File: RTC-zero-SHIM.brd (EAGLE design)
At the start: 30 x 65 mm, 16 parts, among them IC1 DS3231/SO, IC2 DS3231M

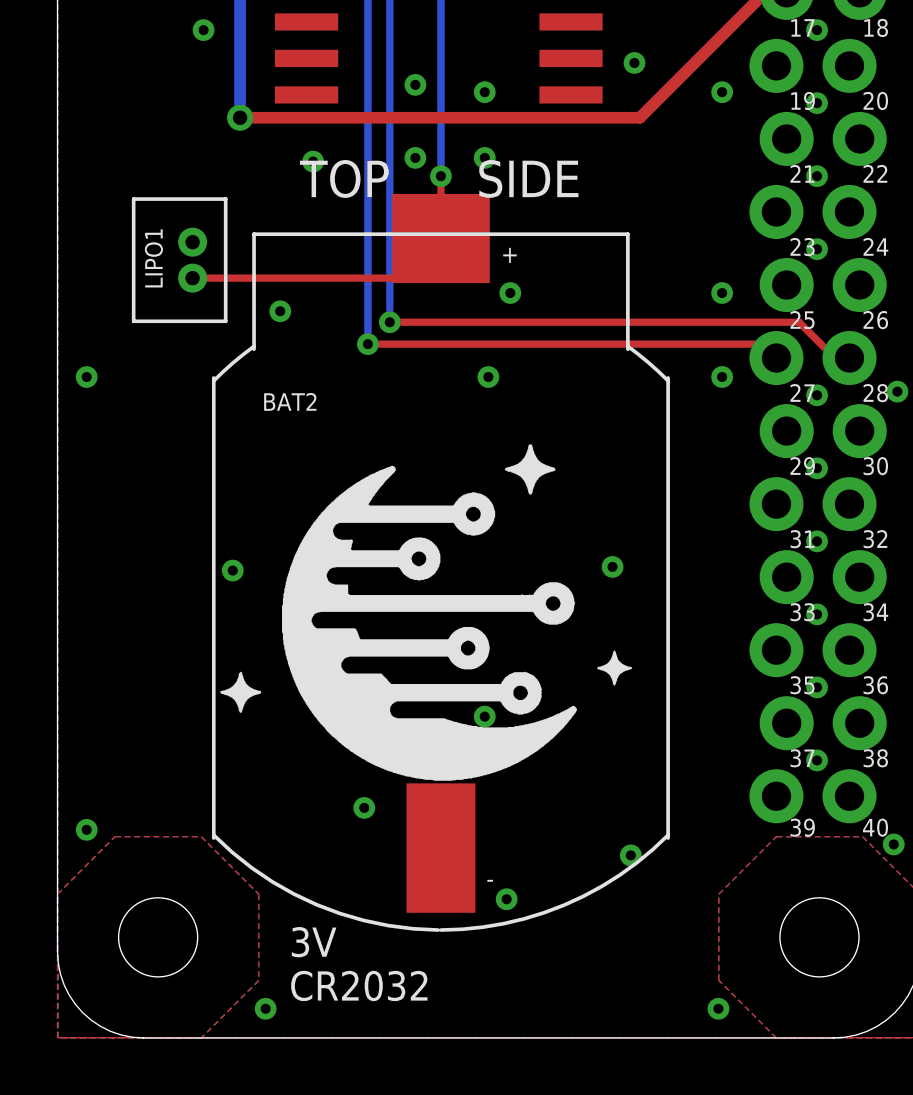
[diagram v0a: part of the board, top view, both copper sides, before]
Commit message: Moved battery holder and lipo connector a bit down to improve compatibility with other boards.
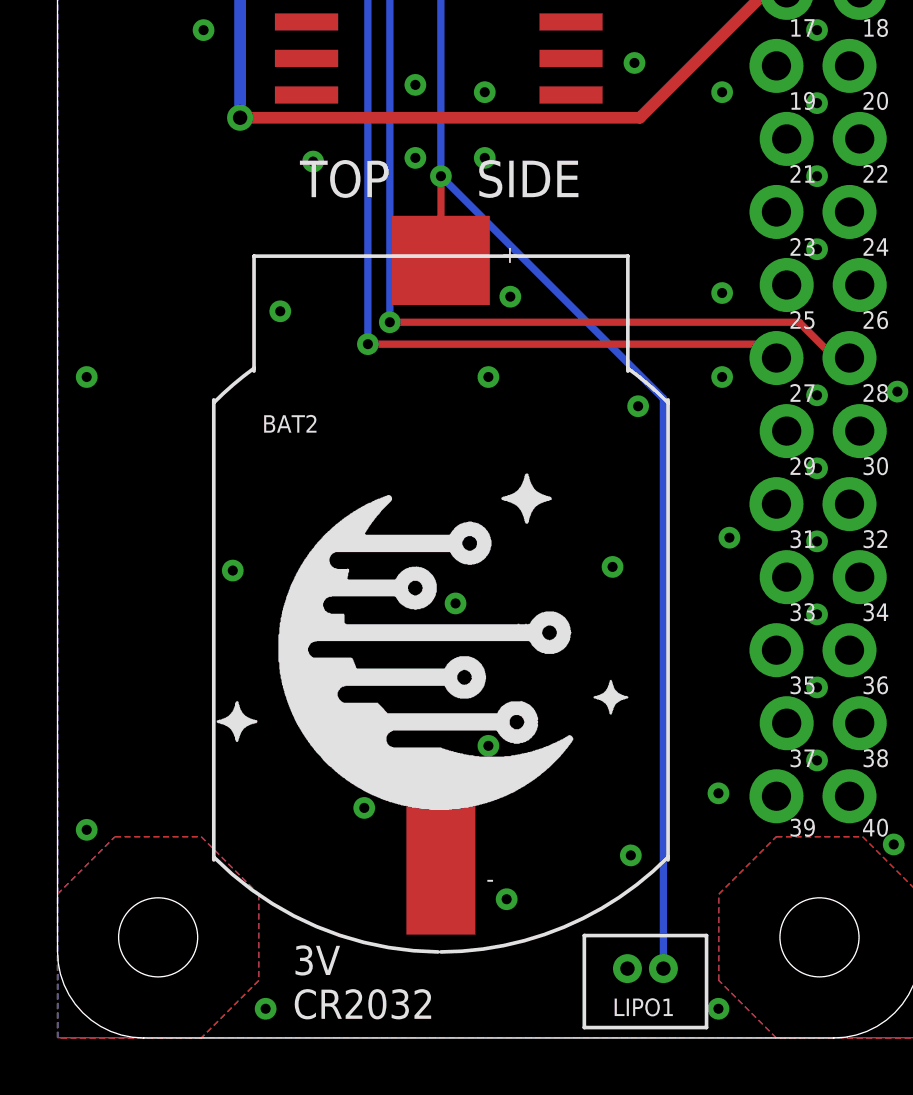
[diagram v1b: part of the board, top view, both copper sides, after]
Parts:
- moved LIPO1 29.2 mm to (20.4, 2.41), turned to 180 degrees
- moved LOGO4 1.02 mm to (4.75, 7.02)
- moved BAT2 0.76 mm to (13.3, 14.2)
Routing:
- net VBAT: track 25.0 -> 47.3 mm
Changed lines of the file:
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@@
 <text x="18.976" y="39.147" size="1.016" layer="22" font="vector" ratio="12" rot="MR0">I2C bus selection</text>
 <rectangle x1="23.912" y1="55.397" x2="26.452" y2="57.937" layer="21"/>
-<text x="8.054" y="1.301" size="1.016" layer="21" font="vector" ratio="12">3V
+<text x="8.181" y="0.666" size="1.016" layer="21" font="vector" ratio="12">3V
 CR2032</text>
 <circle x="7.165" y="42.322" radius="0.127" width="0.2032" layer="21"/>
@@
 <attribute name="VALUE" x="13.3611" y="41.941" size="0.02" layer="28" rot="MR0"/>
 </element>
-<element name="BAT2" library="BS-8-1" package="BS-8-1" value="BS-8-1" x="13.335" y="14.954" smashed="yes" rot="R180">
-<attribute name="NAME" x="7.112" y="21.812" size="0.6096" layer="25" font="vector"/>
-<attribute name="VALUE" x="7.112" y="20.669" size="0.6096" layer="27" font="vector"/>
+<element name="BAT2" library="BS-8-1" package="BS-8-1" value="BS-8-1" x="13.335" y="14.192" smashed="yes" rot="R180">
+<attribute name="NAME" x="7.112" y="21.05" size="0.6096" layer="25" font="vector"/>
+<attribute name="VALUE" x="7.112" y="19.907" size="0.6096" layer="27" font="vector"/>
 </element>
 <element name="LOGO1" library="_my_logos" package="MFDEC_SQ_8MM" value="MFDECLOGO_SQ_8MM" x="7.927" y="51.339" smashed="yes"/>
 <element name="LOGO2" library="_my_logos" package="MFDEC_L_30MM" value="MFDECLOGO_L_30MM" x="-4.138" y="-7.97" smashed="yes" rot="MR90"/>
 <element name="LOGO3" library="_my_logos" package="RSNURL_QR_10MM" value="RSNURL_QR_10MM" x="18.087" y="51.339" smashed="yes" rot="MR0"/>
-<element name="LIPO1" library="PiB_connectors" package="_MOLEX-0530470210_VERT_PITCH-1.25MM" package3d_urn="urn:adsk.eagle:package:2973718/3" value="Molex VERT 1.25mm pitch" x="4.699" y="27.051" smashed="yes" rot="R90">
-<attribute name="DATASHEET_CONNECTOR1" value="https://www.molex.com/pdm_docs/sd/530470210_sd.pdf" x="4.699" y="27.051" size="1.778" layer="27" rot="R90" display="off"/>
-<attribute name="DATASHEET_CONNECTOR2" value="https://www.molex.com/pdm_docs/sd/510210700_sd.pdf" x="4.699" y="27.051" size="1.778" layer="27" rot="R90" display="off"/>
-<attribute name="DATASHEET_CRIMP" value="https://www.molex.com/pdm_docs/sd/500798000_sd.pdf" x="4.699" y="27.051" size="1.778" layer="27" rot="R90" display="off"/>
-<attribute name="DISTLINK_CONNECTOR1" value="https://www.digikey.com/products/en?keywords=WM1731-ND" x="4.699" y="27.051" size="1.778" layer="27" rot="R90" display="off"/>
-<attribute name="DISTLINK_CONNECTOR2" value="https://www.digikey.com/products/en?keywords=WM1720-ND" x="4.699" y="27.051" size="1.778" layer="27" rot="R90" display="off"/>
-<attribute name="DISTLINK_CRIMP" value="https://www.digikey.com/products/en?keywords=WM1142CT-ND" x="4.699" y="27.051" size="1.778" layer="27" rot="R90" display="off"/>
-<attribute name="DISTPN_CONNECTOR1" value="WM1731-ND" x="4.699" y="27.051" size="1.778" layer="27" rot="R90" display="off"/>
-<attribute name="DISTPN_CONNECTOR2" value="WM1720-ND" x="4.699" y="27.051" size="1.778" layer="27" rot="R90" display="off"/>
-<attribute name="DISTPN_CRIMP" value="WM1142CT-ND" x="4.699" y="27.051" size="1.778" layer="27" rot="R90" display="off"/>
-<attribute name="DIST_CONNECTOR1" value="Digikey" x="4.699" y="27.051" size="1.778" layer="27" rot="R90" display="off"/>
-<attribute name="DIST_CONNECTOR2" value="Digikey" x="4.699" y="27.051" size="1.778" layer="27" rot="R90" display="off"/>
-<attribute name="DIST_CRIMP" value="Digikey" x="4.699" y="27.051" size="1.778" layer="27" rot="R90" display="off"/>
-<attribute name="MFR_CONNECTOR1" value="Molex, LLC" x="4.699" y="27.051" size="1.778" layer="27" rot="R90" display="off"/>
-<attribute name="MFR_CONNECTOR2" value="Molex, LLC" x="4.699" y="27.051" size="1.778" layer="27" rot="R90" display="off"/>
-<attribute name="MFR_CRIMP" value="Molex, LLC" x="4.699" y="27.051" size="1.778" layer="27" rot="R90" display="off"/>
-<attribute name="MPN_CONNECTOR1" value="0530470210" x="4.699" y="27.051" size="1.778" layer="27" rot="R90" display="off"/>
-<attribute name="MPN_CONNECTOR2" value="51021-0200" x="4.699" y="27.051" size="1.778" layer="27" rot="R90" display="off"/>
-<attribute name="MPN_CRIMP" value="0500798000" x="4.699" y="27.051" size="1.778" layer="27" rot="R90" display="off"/>
-<attribute name="NAME" x="3.048" y="28.194" size="0.6096" layer="25" font="vector" rot="R270"/>
+<element name="LIPO1" library="PiB_connectors" package="_MOLEX-0530470210_VERT_PITCH-1.25MM" package3d_urn="urn:adsk.eagle:package:2973718/3" value="Molex VERT 1.25mm pitch" x="20.447" y="2.413" smashed="yes" rot="R180">
+<attribute name="DATASHEET_CONNECTOR1" value="https://www.molex.com/pdm_docs/sd/530470210_sd.pdf" x="20.447" y="2.413" size="1.778" layer="27" rot="R180" display="off"/>
+<attribute name="DATASHEET_CONNECTOR2" value="https://www.molex.com/pdm_docs/sd/510210700_sd.pdf" x="20.447" y="2.413" size="1.778" layer="27" rot="R180" display="off"/>
+<attribute name="DATASHEET_CRIMP" value="https://www.molex.com/pdm_docs/sd/500798000_sd.pdf" x="20.447" y="2.413" size="1.778" layer="27" rot="R180" display="off"/>
+<attribute name="DISTLINK_CONNECTOR1" value="https://www.digikey.com/products/en?keywords=WM1731-ND" x="20.447" y="2.413" size="1.778" layer="27" rot="R180" display="off"/>
+<attribute name="DISTLINK_CONNECTOR2" value="https://www.digikey.com/products/en?keywords=WM1720-ND" x="20.447" y="2.413" size="1.778" layer="27" rot="R180" display="off"/>
+<attribute name="DISTLINK_CRIMP" value="https://www.digikey.com/products/en?keywords=WM1142CT-ND" x="20.447" y="2.413" size="1.778" layer="27" rot="R180" display="off"/>
+<attribute name="DISTPN_CONNECTOR1" value="WM1731-ND" x="20.447" y="2.413" size="1.778" layer="27" rot="R180" display="off"/>
+<attribute name="DISTPN_CONNECTOR2" value="WM1720-ND" x="20.447" y="2.413" size="1.778" layer="27" rot="R180" display="off"/>
+<attribute name="DISTPN_CRIMP" value="WM1142CT-ND" x="20.447" y="2.413" size="1.778" layer="27" rot="R180" display="off"/>
+<attribute name="DIST_CONNECTOR1" value="Digikey" x="20.447" y="2.413" size="1.778" layer="27" rot="R180" display="off"/>
+<attribute name="DIST_CONNECTOR2" value="Digikey" x="20.447" y="2.413" size="1.778" layer="27" rot="R180" display="off"/>
+<attribute name="DIST_CRIMP" value="Digikey" x="20.447" y="2.413" size="1.778" layer="27" rot="R180" display="off"/>
+<attribute name="MFR_CONNECTOR1" value="Molex, LLC" x="20.447" y="2.413" size="1.778" layer="27" rot="R180" display="off"/>
+<attribute name="MFR_CONNECTOR2" value="Molex, LLC" x="20.447" y="2.413" size="1.778" layer="27" rot="R180" display="off"/>
+<attribute name="MFR_CRIMP" value="Molex, LLC" x="20.447" y="2.413" size="1.778" layer="27" rot="R180" display="off"/>
+<attribute name="MPN_CONNECTOR1" value="0530470210" x="20.447" y="2.413" size="1.778" layer="27" rot="R180" display="off"/>
+<attribute name="MPN_CONNECTOR2" value="51021-0200" x="20.447" y="2.413" size="1.778" layer="27" rot="R180" display="off"/>
+<attribute name="MPN_CRIMP" value="0500798000" x="20.447" y="2.413" size="1.778" layer="27" rot="R180" display="off"/>
+<attribute name="NAME" x="19.304" y="0.762" size="0.6096" layer="25" font="vector"/>
 </element>
 <element name="IC2" library="SparkFun-Clocks" library_urn="urn:adsk.eagle:library:511" package="SO08" package3d_urn="urn:adsk.eagle:package:37530/1" value="DS3231M" x="13.261" y="39.782" smashed="yes" rot="R270">
@@
 <attribute name="VALUE" x="14.785" y="38.004" size="0.6096" layer="27" font="vector" rot="R90"/>
 </element>
-<element name="LOGO4" library="_my_logos" package="MFDEC_L_10MM" value="MFDECLOGO_L_10MM" x="4.879" y="8.032" smashed="yes"/>
+<element name="LOGO4" library="_my_logos" package="MFDEC_L_10MM" value="MFDECLOGO_L_10MM" x="4.752" y="7.016" smashed="yes"/>
 </elements>
 <signals>
@@
 <contactref element="IC2" pad="6"/>
 <wire x1="17.861" y1="39.147" x2="16.061" y2="39.147" width="0.254" layer="1"/>
-<wire x1="13.335" y1="27.804" x2="11.957" y2="26.426" width="0.254" layer="1"/>
-<wire x1="11.957" y1="26.426" x2="4.699" y2="26.426" width="0.254" layer="1"/>
 <via x="13.335" y="29.972" extent="1-16" drill="0.35"/>
-<wire x1="13.335" y1="29.972" x2="13.335" y2="27.804" width="0.254" layer="1"/>
+<wire x1="13.335" y1="29.972" x2="13.335" y2="27.042" width="0.254" layer="1"/>
 <wire x1="13.335" y1="29.972" x2="13.335" y2="38.989" width="0.254" layer="16"/>
 <via x="13.335" y="38.989" extent="1-16" drill="0.35"/>
@@
 <wire x1="15.934" y1="39.02" x2="16.061" y2="39.147" width="0.254" layer="1"/>
 <wire x1="15.934" y1="39.02" x2="13.366" y2="39.02" width="0.254" layer="1"/>
+<wire x1="21.072" y1="2.413" x2="21.072" y2="22.235" width="0.254" layer="16"/>
+<wire x1="21.072" y1="22.235" x2="13.335" y2="29.972" width="0.254" layer="16"/>
 </signal>
 <signal name="SCL">
@@
 <via x="19.939" y="6.35" extent="1-16" drill="0.35"/>
 <via x="10.668" y="8.001" extent="1-16" drill="0.35"/>
-<via x="14.859" y="11.176" extent="1-16" drill="0.35"/>
+<via x="14.986" y="10.16" extent="1-16" drill="0.35"/>
 <via x="15.621" y="4.826" extent="1-16" drill="0.35"/>
 <via x="1.016" y="40.513" extent="1-16" drill="0.35"/>
@@
 <via x="7.747" y="25.273" extent="1-16" drill="0.35"/>
 <via x="14.986" y="22.987" extent="1-16" drill="0.35"/>
-<via x="15.748" y="25.908" extent="1-16" drill="0.35"/>
+<via x="15.748" y="25.781" extent="1-16" drill="0.35"/>
 <via x="23.114" y="22.987" extent="1-16" drill="0.35"/>
 <via x="23.114" y="25.908" extent="1-16" drill="0.35"/>
@@
 <via x="6.096" y="16.256" extent="1-16" drill="0.35"/>
 <via x="19.304" y="16.383" extent="1-16" drill="0.35"/>
+<via x="22.987" y="8.509" extent="1-16" drill="0.35"/>
+<via x="23.368" y="17.399" extent="1-16" drill="0.35"/>
+<via x="20.193" y="21.971" extent="1-16" drill="0.35"/>
+<via x="13.843" y="15.113" extent="1-16" drill="0.35"/>
 </signal>
 <signal name="SCL0">
